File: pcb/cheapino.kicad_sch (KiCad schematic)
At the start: 17 parts, among them U10 TXS0101DBV

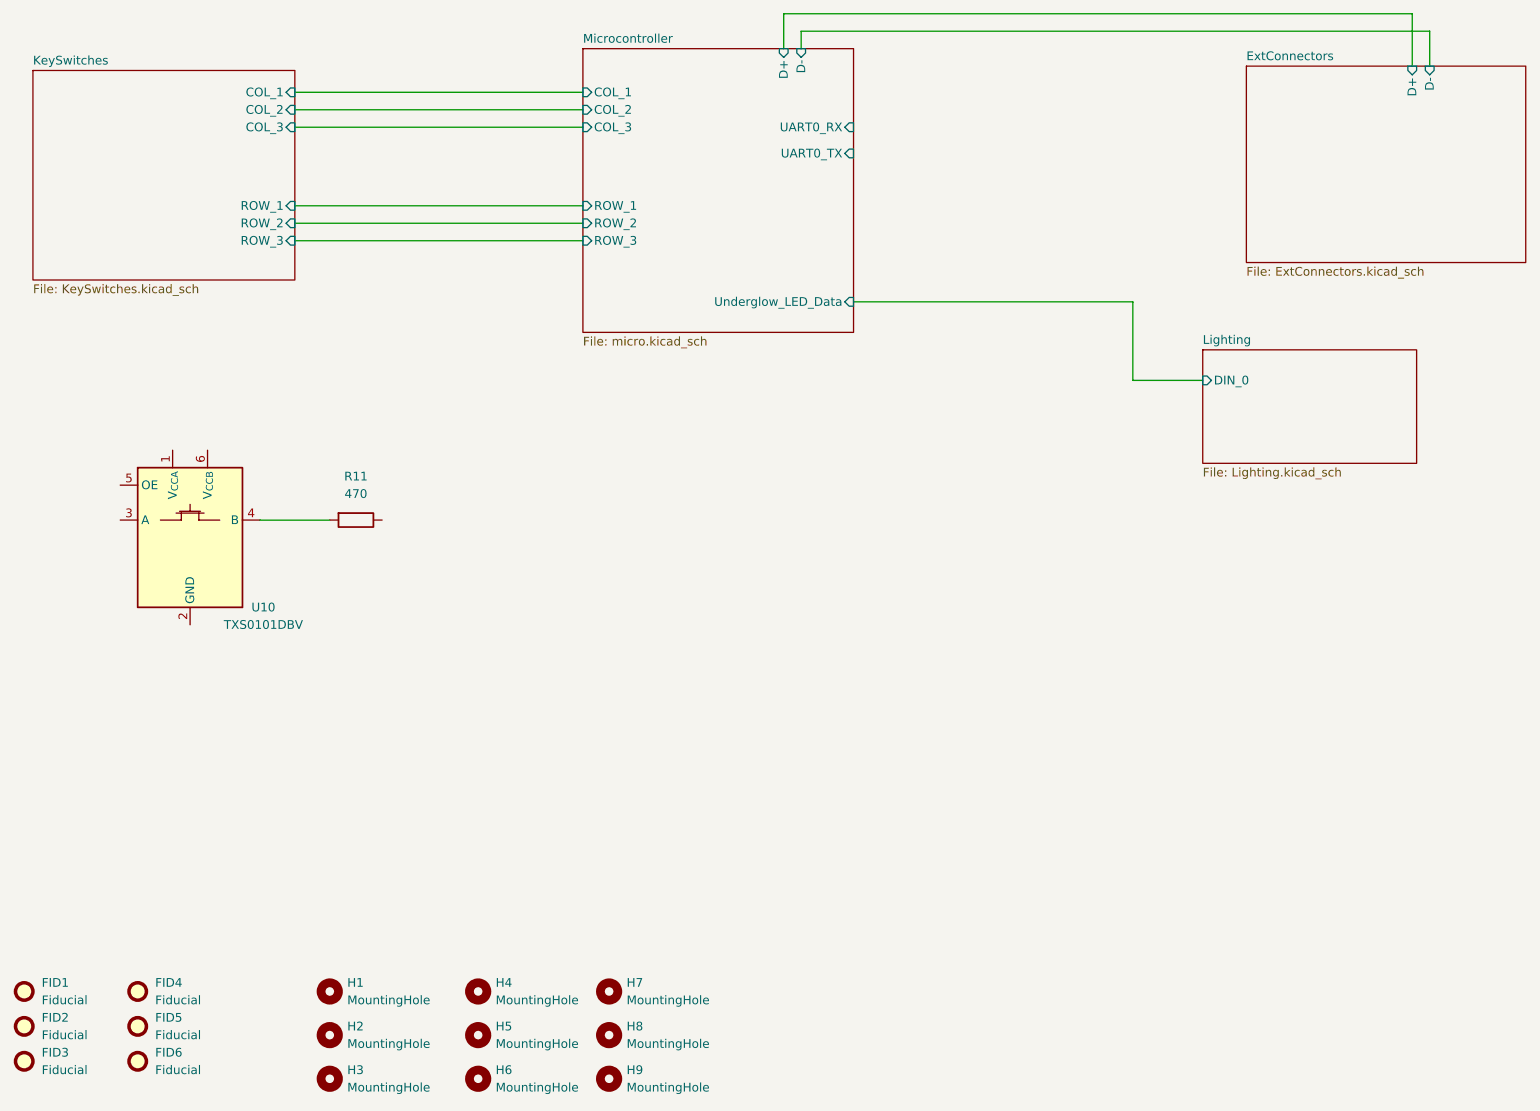
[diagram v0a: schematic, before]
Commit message: WIP: Updating keyboard matrix to use the new shared part and reorganizing all the LED outputs.
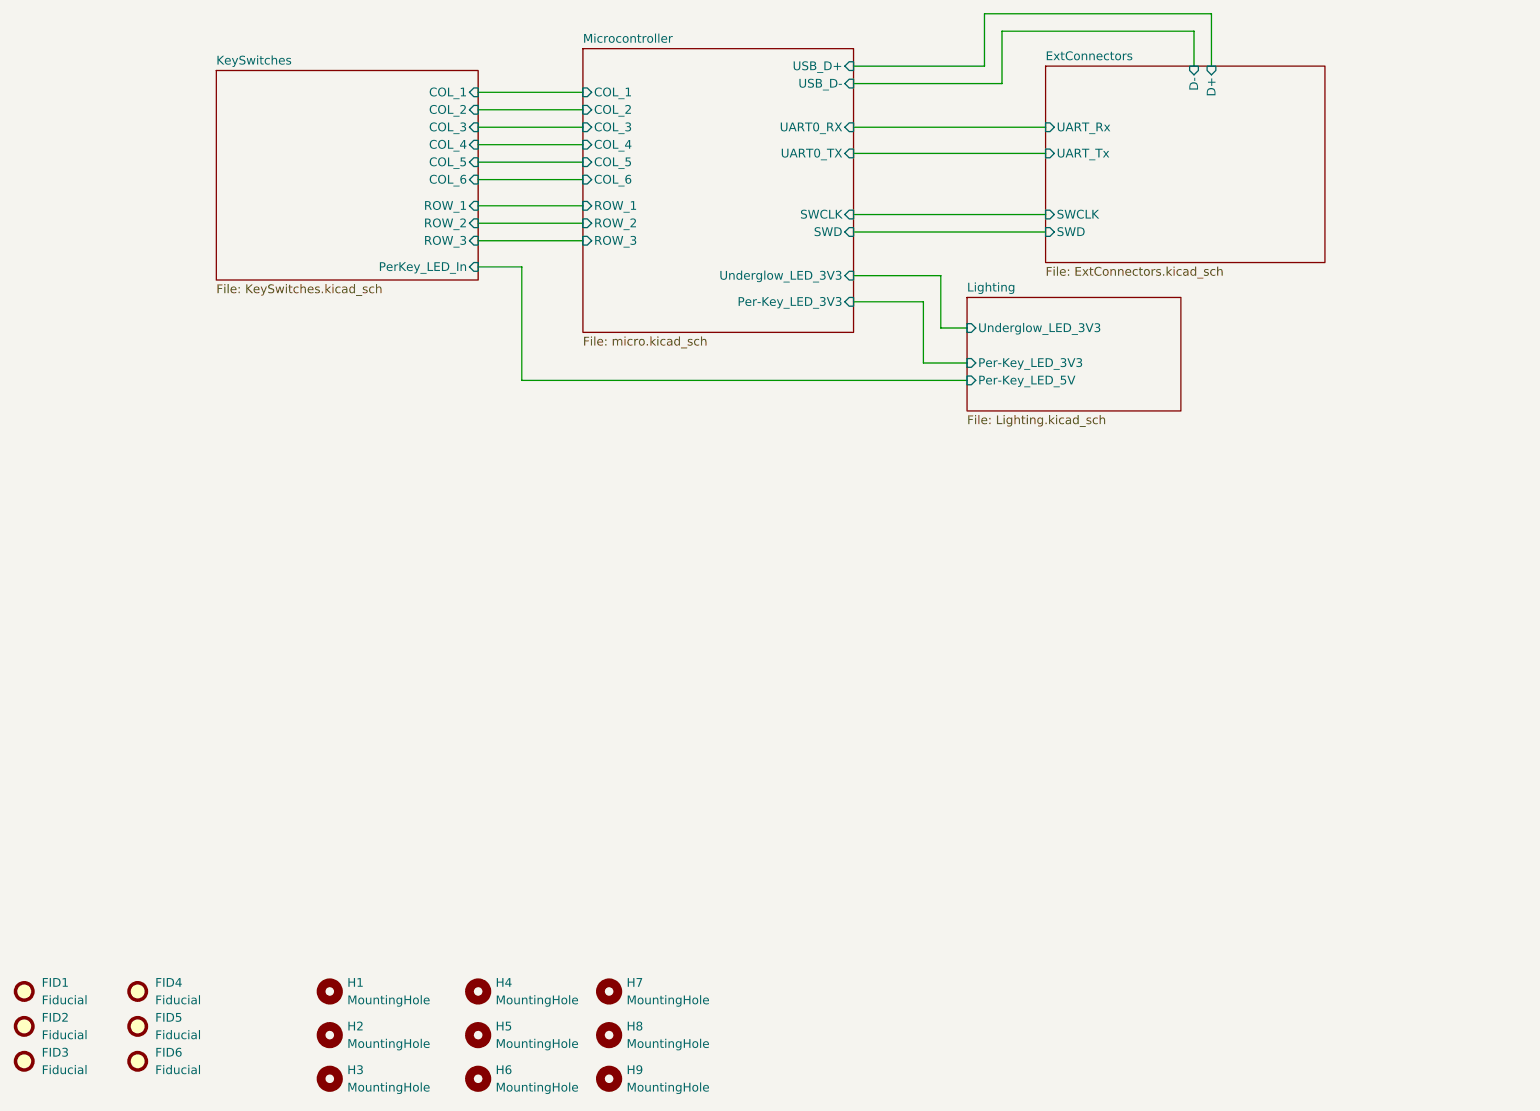
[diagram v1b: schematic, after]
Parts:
- removed R11: 470, Resistor_SMD:R_0603_1608Metric_Pad0.98x0.95mm_HandSolder, symbol Device:R
- removed U10: TXS0101DBV, Package_TO_SOT_SMD:SOT-23-6, symbol Logic_LevelTranslator:TXS0101DBV
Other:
- sheet ExtConnectors ports: added SWCLK, SWD, UART_Rx, UART_Tx; removed none
- sheet KeySwitches ports: added COL_4, COL_5, COL_6, PerKey_LED_In; removed none
- sheet Lighting ports: added Per-Key_LED_3V3, Per-Key_LED_5V, Underglow_LED_3V3; removed DIN_0
- sheet Microcontroller ports: added COL_4, COL_5, COL_6, Per-Key_LED_3V3, SWCLK, SWD, USB_D+, USB_D-, Underglow_LED_3V3; removed D+, D-, Underglow_LED_Data

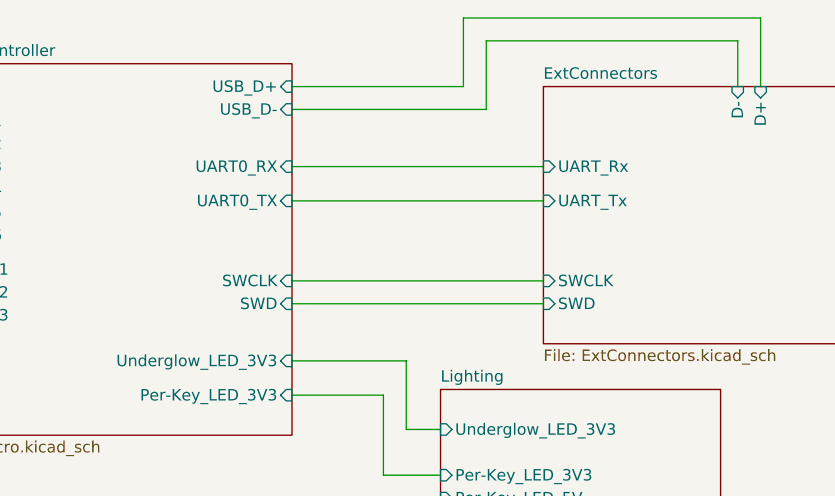
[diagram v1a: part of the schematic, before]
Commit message: Adding reversible MX Sockets and SK6812MiniE footprints, finishing the replacement of Ethernet with a TRRS connector and selectable 0Ohm resistors to swap Rx/Tx for the interconnect.
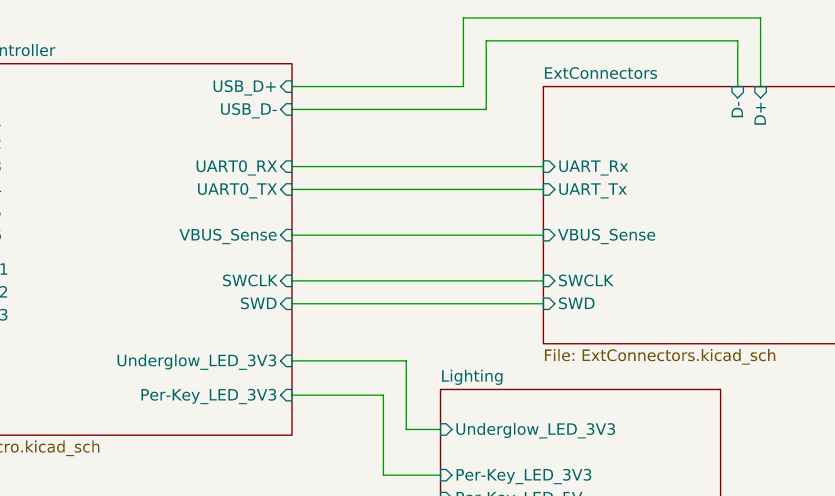
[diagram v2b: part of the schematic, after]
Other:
- sheet ExtConnectors ports: added VBUS_Sense; removed none
- sheet Microcontroller ports: added VBUS_Sense; removed none
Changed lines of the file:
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@@
+	(wire
+		(pts
+			(xy 152.4 57.15) (xy 180.34 57.15)
+		)
+		(stroke
+			(width 0)
+			(type default)
+		)
+	)
 	(wire
 		(pts
@@
 	(wire
 		(pts
-			(xy 152.4 53.34) (xy 180.34 53.34)
+			(xy 152.4 52.07) (xy 180.34 52.07)
 		)
 		(stroke
@@
 		)
 		(pin "UART0_TX" input
-			(at 152.4 53.34 0)
+			(at 152.4 52.07 0)
 			(effects
 				(font
@@
 		(pin "USB_D-" input
 			(at 152.4 43.18 0)
+			(effects
+				(font
+					(size 1.27 1.27)
+				)
+				(justify right)
+			)
+		)
+		(pin "VBUS_Sense" input
+			(at 152.4 57.15 0)
 			(effects
 				(font
@@
 		)
 		(pin "UART_Tx" input
-			(at 180.34 53.34 180)
-			(effects
-				(font
+			(at 180.34 52.07 180)
+			(effects
+				(font
+					(size 1.27 1.27)
+				)
+				(justify left)
+			)
+		)
+		(pin "VBUS_Sense" input
+			(at 180.34 57.15 180)
+			(effects
+				(font
